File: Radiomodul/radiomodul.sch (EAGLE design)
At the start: 46 parts, among them IC1 MCP601R, IC2 AD5243, IC3 TXS0104, IC4 TXB0104PWR, IC5 NCV4274CSOT-223, IC6 E910.15, IC7 NCV4274CSOT-223, Q1 12MHz, U1 LPC1343FBD48, U2 MCP130T

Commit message: MFL Radio interface done.
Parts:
- removed C5: 330pF, rcl:C-EUC0805
- removed D2: S1J, Heinrich:DIODESMA
- removed D4: SMBJ36A, diode:SUPPRESSOR-SMBJ
- removed JTAG1: SWD, microbuilder:JTAG-CORTEXM3
- removed LED1: Power, led:LEDSML0805
- removed R11: 620k, rcl:R-EU_R0805
- removed R12: 100k, rcl:R-EU_R0805
- removed R13: 100, rcl:R-EU_R0805
- removed U1: LPC1343FBD48, nxp_60_1_1:LPC1343FBD48
- removed U2: MCP130T, microbuilder:MCP130TWAVE
- added D3: (no value), Heinrich:DIODESMA
- added J1: 39-30-1100, Heinrich:39-30-1100
- added L1: 10µH, Heinrich:FERRITE1206
- C1, C2: value 22pF -> 100nF
- C10: value 100nF -> 100pF
- C11: value 100nF -> 10nF
- C12: value 100nF -> 330pF
- C13: device rcl:C-EUC1210 -> rcl:C-EUC0805
- C14: value 100pF -> 100nF
- C15: value 100nF -> 10µF; device rcl:C-EUC1210 -> rcl:CPOL-EUD
- C16: value 10µF/50V -> 47nF; device rcl:CPOL-EUD -> rcl:C-EUC0805
- C17: value 100nF -> 22µF; device rcl:C-EUC0805 -> rcl:C-EUC1206
- C18: value 10µF -> 18pF; device Heinrich:CAP_TANTALUMSMCA -> rcl:C-EUC0805
- C19: value 100nF -> 18pF
- C20: value 10µF -> 100nF; device rcl:C-EUC1210 -> rcl:C-EUC0805
- C21: value 22µF -> 100nF; device rcl:C-EUC1210 -> rcl:C-EUC0805
- C6: value 10nF -> 100nF
- D1: value SMBJ36CA -> SMBJ28A; device Heinrich:P6SMBXXCA -> Heinrich:P6SMBXXASMB
- IC1: value MCP601R -> ATMEGA2561-16AI; device linear:MCP601R -> atmel-2005:ATMEGA2561-16AI
- IC2: value AD5243 -> MCP42050; device Heinrich:AD5243 -> Heinrich:MCP42050
- IC3: value TXS0104 -> E910.15; device Heinrich:TXS0104 -> Heinrich:E910.15
- IC4: value TXB0104PWR -> AVR-JTAG; device Heinrich:TXB0104PWR -> Heinrich:AVR-JTAG
- IC5: value NCV4274CSOT-223 -> MAX232ECWE; device Heinrich:NCV4274CSOT-223 -> maxim:MAX232ECWE
- IC6: value E910.15 -> MCP601SN; device Heinrich:E910.15 -> linear:MCP601SN
- IC7: value NCV4274CSOT-223 -> TLE42754D; device Heinrich:NCV4274CSOT-223 -> Heinrich:TLE42754D
- Q1: value 12MHz -> 14,7456
- R1: value 10k -> 10
- R2: value 10k -> 4k7
- R3: value 10k -> 100
- R4: value 56 -> 100k
- R5: value 10 -> 180k
- R6: value 10k -> 5k
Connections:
- removed net /SEN: IC4.A3, U1.PIO0_7/!CTS!, U1.PIO2_1/!DSR!
- removed net 3.3V: C11.1, C12.1, C20.1, C3.1, C4.1, C8.1, C9.1, IC1.V+, IC3.OE, IC3.VCCA, IC4.OE, IC4.VCCA, IC5.OUT, JTAG1.1, R2.2, R3.2, R4.2, R6.2, U1.VDD, U2.VCC
- removed net ADC: C6.1, R13.2, U1.R/PIO1_1/AD2/CT32B1_MAT0
- removed net N$2: IC1.-IN, IC1.OUT, R13.1
- removed net N$3: IC2.SCL, IC3.B2
- removed net RING: IC3.A3, U1.PIO0_3/USB_VBUS
- removed net RXD: IC4.A1, U1.PIO1_6/RXD/CT32B0_MAT0
- removed net R_RING: IC3.B3
- removed net R_SLEEVE: IC2.W2
- removed net R_TIP: IC2.A1
- removed net SCL: IC3.A2, U1.PIO0_4/SCL
- removed net SDA: IC3.A1, U1.PIO0_5/SDA
- removed net SWCLK: JTAG1.4, R1.1, U1.SWCLK/PIO0_10/SCK0/CT16B0_MAT2
- removed net SWDIO: JTAG1.2, R2.1, U1.SWDIO/PIO1_3/AD4/CT32B1_MAT2
- removed net SWO: JTAG1.6, R3.1, U1.PIO0_9/MOSI0/CT16B0_MAT1/SWO
- removed net TXD: IC4.A2, U1.PIO1_7/TXD/CT32B0_MAT1
- removed net VCC: C13.1, C15.1, D2.A, IC5.IN, IC7.IN
- removed net XTALIN: C1.1, Q1.2, U1.XTALIN
- removed net XTALOUT: C2.2, Q1.1, U1.XTALOUT
- new net /CS: IC1.(SS/PCINT0)PB0, IC2./CS
- new net ADC0: C11.1, IC1.(ADC0)PF0, R3.2
- new net AREF: C2.1, IC1.AREF
- new net AVCC: IC1.AVCC, L1.P$2
- new net BECKER_RXD: IC5G$1.R1IN, J1.6
- new net BECKER_TXD: IC5G$1.T1OUT, J1.1
- new net BRXD: IC1.(RXD1/INT2)PD2, IC5G$1.R1OUT
- new net BTXD: IC1.(TXD1/INT3)PD3, IC5G$1.T1IN
- new net BUS: C10.1, IC3.BUS, R1.1
- new net IRXD: IC1.(RXD0/PCIN8/PDI)PE0, IC3.RXD
- new net ISEN: IC1.(XCK0/AIN0)PE2, IC3.SEN/STA
- new net ITXD: IC1.(TXD0/PDO)PE1, IC3.TXD
- new net MISO: IC1.(MISO/PCINT3)PB3, IC2.SO
- new net MOSI: IC1.(MOSI/PCINT2)PB2, IC2.SI
- new net N$11: C7.2, IC5G$1.C1+
- new net N$14: C16.1, IC7.D
- new net PIONEER_1: IC2.PA1, J1.7
- new net PIONEER_2: IC1.(OC2A/PCINT4)PB4, J1.8
- new net PIONEER_3: IC2.PW0, J1.3
- new net SAFT: C14.1, C15.+, D1.C, D3.C, IC7.I, R2.2
- new net SCK: IC1.(SCK/PCINT1)PB1, IC2.SCK
- new net TCK: IC1.(ADC4/TCK)PF4, IC4.TCK
- new net TDI: IC1.(ADC7/TDI)PF7, IC4.TDI
- new net TDO: IC1.(ADC6/TDO)PF6, IC4.TDO
- new net TMS: IC1.(ADC5/TMS)PF5, IC4.TMS
- new net XTAL1: C19.2, IC1.XTAL1, Q1.1
- new net XTAL2: C18.1, IC1.XTAL2, Q1.2
- net +12V: now also D3.A, J1.5; no longer C16.+, D1.2
- net /RESET: now also IC1.RESET, IC4./RESET, IC7.RO; no longer JTAG1.10, U1.!RESET!/PIO0_0, U2.RST
- net 5.0V: now also C1.1, C13.1, C20.1, C3.1, C4.1, C6.1, IC1.VCC, IC1.VCC1, IC3.VCC, IC4.VCC, IC5P.VCC, IC6.V+, IC7.Q, L1.P$1, R6.2; no longer C10.1, C18.+, C22.1, C7.1, IC3.VCCB, IC4.VCCB, IC6.VCC, IC7.OUT
- net GND: now also C15.-, C16.2, C18.2, C19.1, C2.2, D1.A, IC1.AGND, IC1.GND, IC1.GND1, IC2.VSS, IC4.GND@1, IC4.GND@2, IC5P.GND, IC6.V-, J1.2, J1.4, R4.1; no longer C15.2, C16.-, C18.-, C19.2, C2.1, C5.2, C7.2, C8.2, C9.2, D1.1, D4.A, IC1.V-, IC2.GND, IC5.GND, IC6.GND, JTAG1.3, JTAG1.5, JTAG1.9, LED1.C, R1.2, R12.1, U1.VSS, U2.GND
- net IBUS: now also J1.9, R1.2, R2.1; no longer R5.2
- net LICHT: now also J1.10, R5.2; no longer R11.2
- net N$1: now also IC2.PA0, IC2.PW1; no longer IC2.SDA, IC3.B1
- net N$10: now also C9.1, IC5G$1.V+; no longer IC4.B3, IC6.SEN/STA
- net N$4: now also C7.1, IC5G$1.C1-; no longer LED1.A, R4.1
- net N$5: now also C12.1, IC6.+IN, R4.2, R5.1; no longer IC4.B1, IC6.RXD
- net N$6: now also C8.1, IC5G$1.C2-; no longer IC2.A2, IC2.W1
- net N$7: now also IC6.-IN, IC6.OUT, R3.1; no longer IC4.B2, IC6.TXD
- net N$8: now also C8.2, IC5G$1.C2+; no longer C5.1, IC1.+IN, R11.1, R12.2
- net N$9: now also C9.2, IC5G$1.V-; no longer C14.1, IC6.BUS, R5.1
- net VBAT: now also C22.1, IC3.VBAT; no longer C19.1, D2.C, D4.C, IC6.VBAT
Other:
- note removed: "LED1: EVL 17-21/S2C-A Orange, 20mA, 2,35V"

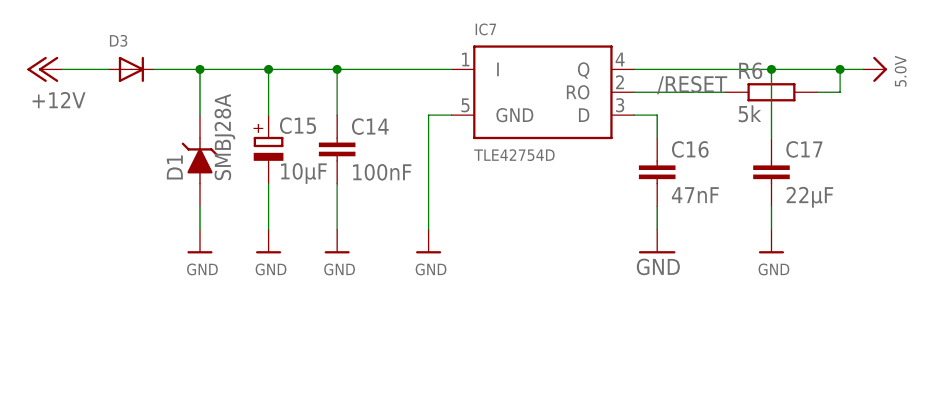
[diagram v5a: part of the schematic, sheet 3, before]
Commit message: some parts changed, BOM added
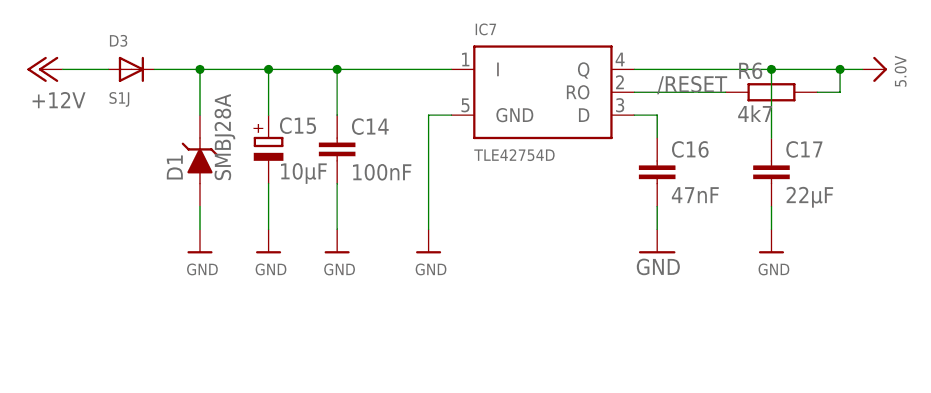
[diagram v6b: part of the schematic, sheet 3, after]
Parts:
- D3: value (none) -> S1J
- Q1: value 14,7456 -> 16000000
- R6: value 5k -> 4k7
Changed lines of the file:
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@@
 <part name="U$33" library="microbuilder" deviceset="GND" device=""/>
 <part name="U$34" library="microbuilder" deviceset="5.0V" device=""/>
-<part name="R6" library="rcl" library_urn="urn:adsk.eagle:library:334" deviceset="R-EU_" device="R0805" package3d_urn="urn:adsk.eagle:package:23553/2" value="5k"/>
-<part name="Q1" library="crystal" library_urn="urn:adsk.eagle:library:204" deviceset="CRYSTAL" device="HC49UP" package3d_urn="urn:adsk.eagle:package:12078/1" value="14,7456"/>
+<part name="R6" library="rcl" library_urn="urn:adsk.eagle:library:334" deviceset="R-EU_" device="R0805" package3d_urn="urn:adsk.eagle:package:23553/2" value="4k7"/>
+<part name="Q1" library="crystal" library_urn="urn:adsk.eagle:library:204" deviceset="CRYSTAL" device="HC49UP" package3d_urn="urn:adsk.eagle:package:12078/1" value="16000000"/>
 <part name="C18" library="rcl" library_urn="urn:adsk.eagle:library:334" deviceset="C-EU" device="C0805" package3d_urn="urn:adsk.eagle:package:23617/2" value="18pF"/>
 <part name="C19" library="rcl" library_urn="urn:adsk.eagle:library:334" deviceset="C-EU" device="C0805" package3d_urn="urn:adsk.eagle:package:23617/2" value="18pF"/>
@@
 <part name="C22" library="rcl" library_urn="urn:adsk.eagle:library:334" deviceset="C-EU" device="C0805" package3d_urn="urn:adsk.eagle:package:23617/2" value="100nF"/>
 <part name="U$32" library="microbuilder" deviceset="GND" device=""/>
-<part name="D3" library="Heinrich" deviceset="DIODE" device="SMA"/>
+<part name="D3" library="Heinrich" deviceset="DIODE" device="SMA" value="S1J"/>
 <part name="J1" library="Heinrich" deviceset="39-30-1100" device=""/>
 <part name="P+3" library="supply1" library_urn="urn:adsk.eagle:library:371" deviceset="+12V" device=""/>
